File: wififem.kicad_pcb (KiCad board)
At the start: 2 copper layers, 31 parts, among them J1 Conn_Coaxial, J2 Conn_Coaxial, J3 Conn_Coaxial, J4 Conn_Coaxial, U1 MCP6566, U2 74HCT04, U3 SE2611T

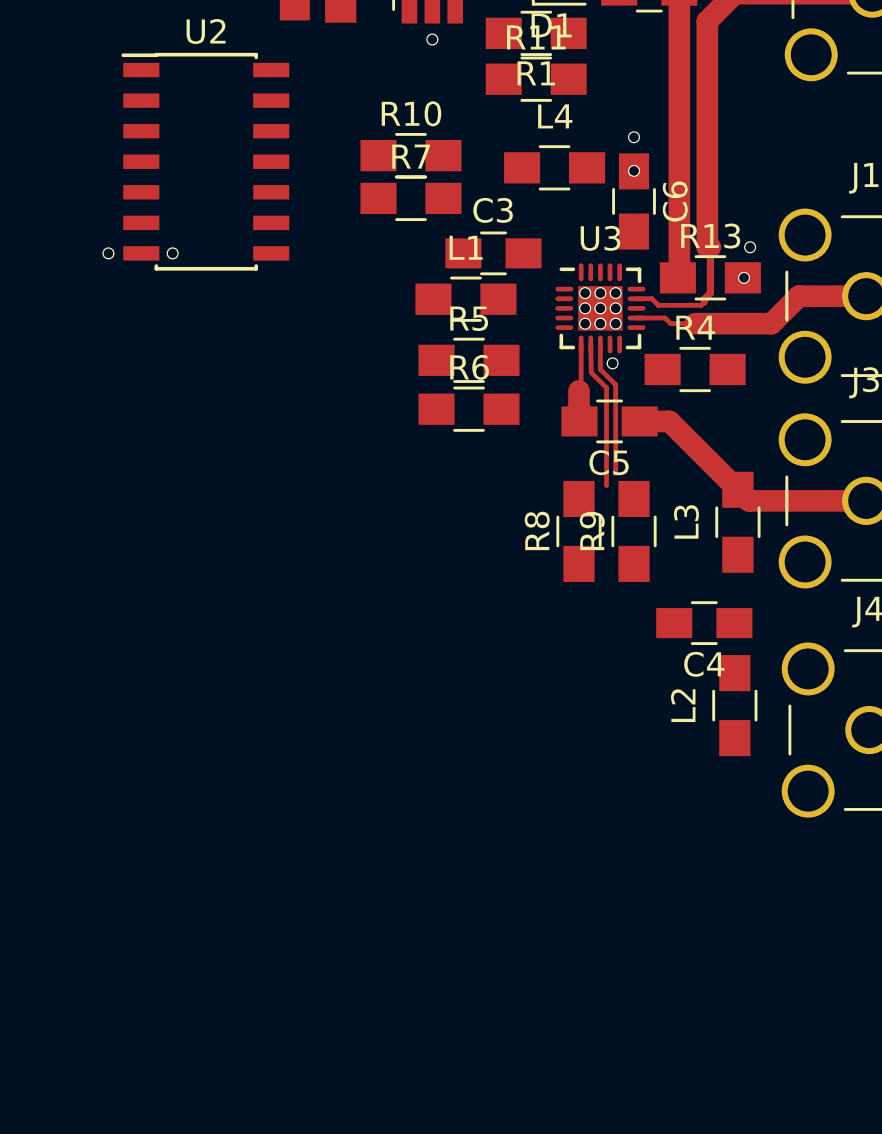
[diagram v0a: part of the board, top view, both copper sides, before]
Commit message: Add regulator in schematic, some progress with layout
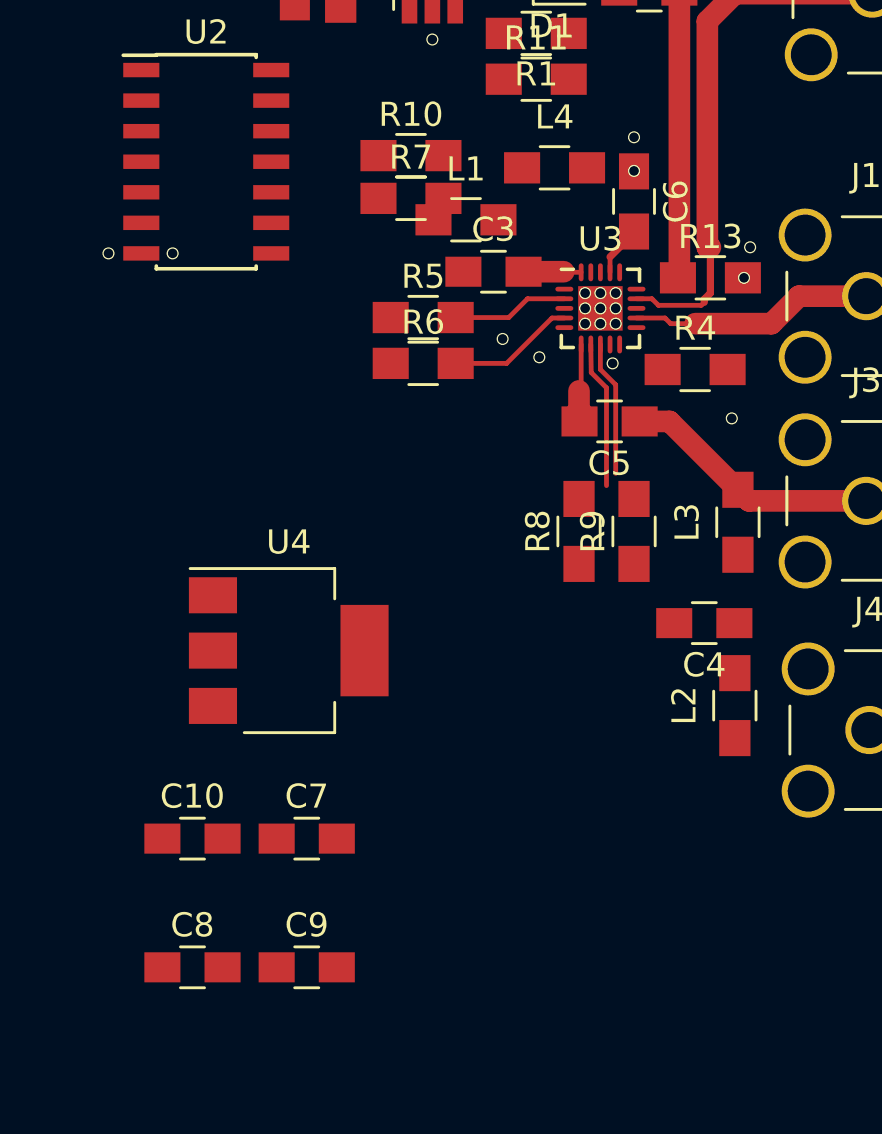
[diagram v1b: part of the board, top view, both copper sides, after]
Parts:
- added C10: 100n, Capacitors_SMD:C_0805_HandSoldering, F.Cu at (92.9, 87.4)
- added C7: 100n, Capacitors_SMD:C_0805_HandSoldering, F.Cu at (97.6, 87.4)
- added C8: 100n, Capacitors_SMD:C_0805_HandSoldering, F.Cu at (92.9, 92.8)
- added C9: 100n, Capacitors_SMD:C_0805_HandSoldering, F.Cu at (97.6, 92.8)
- added U4: AP1117-15, TO_SOT_Packages_SMD:SOT-223-3_TabPin2, F.Cu at (96.9, 79.6)
- moved L1 3.30 mm to (104.3, 61.7)
- moved R6 2.69 mm to (102.5, 67.7)
- moved R5 2.61 mm to (102.5, 65.8)
- moved C3 0.76 mm to (105.4, 63.9)
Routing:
- net Net-(R6-Pad2): track 0.00 -> 5.30 mm
- net Net-(R5-Pad2): track 0.00 -> 4.84 mm
- net Net-(C3-Pad2): track 0.00 -> 2.40 mm
- net Net-(C6-Pad2): track 0.00 -> 2.11 mm
- net GND: vias 20 -> 23

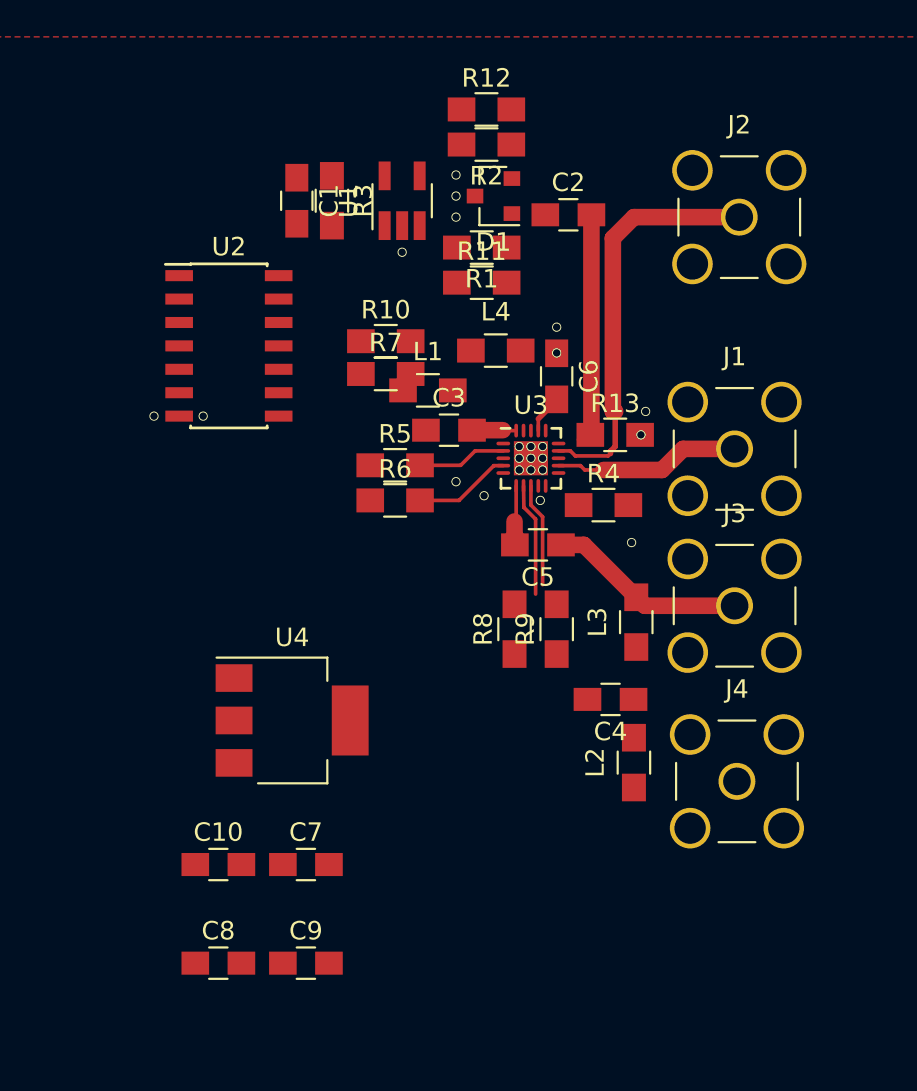
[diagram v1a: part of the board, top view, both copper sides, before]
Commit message: Replaced directional coupler with simple parallel connection. Layout almost done
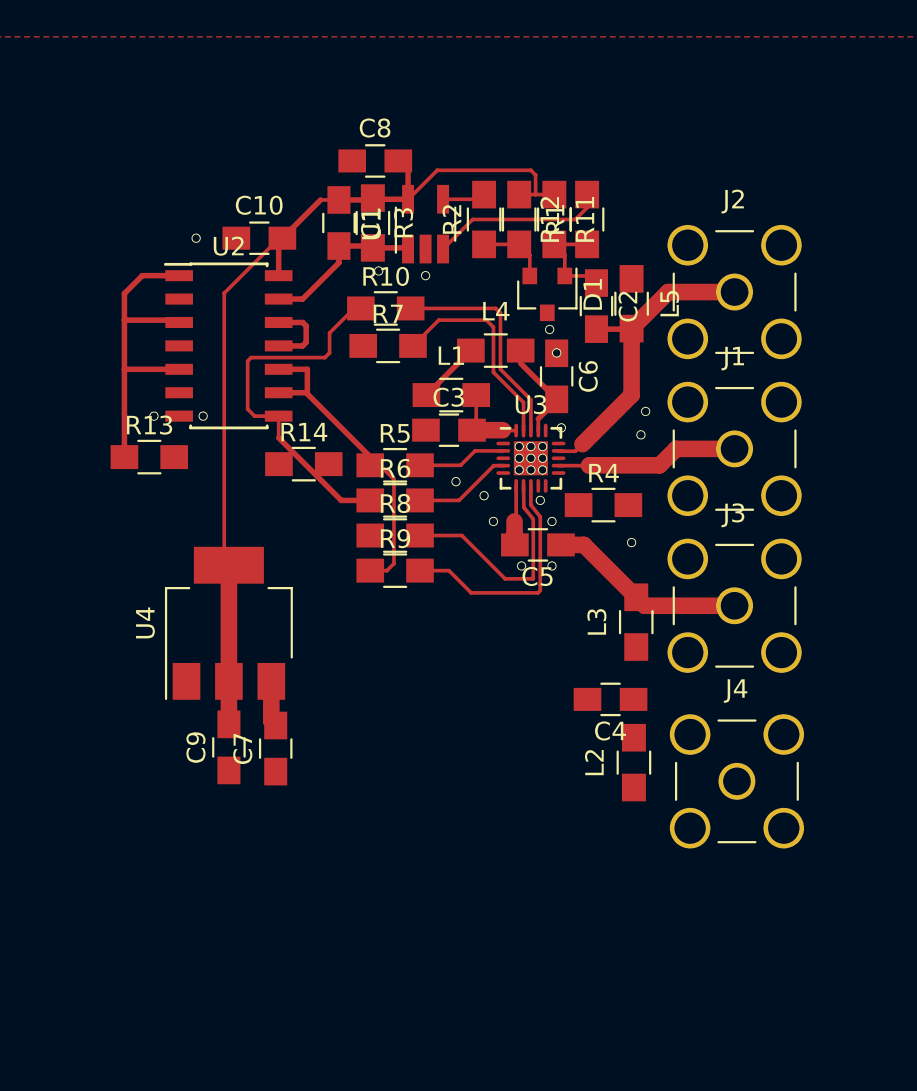
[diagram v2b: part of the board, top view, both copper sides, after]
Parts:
- added L5: 10n, Inductors_SMD:L_0805_HandSoldering, F.Cu at (115.3, 57.0)
- added R14: 0, Resistors_SMD:R_0805_HandSoldering, F.Cu at (97.5, 65.7)
- C2: value 10p -> 1p
- L1, L2, L3, L4: value INDUCTOR -> 2.4 GHz choke
- moved C8 44.3 mm to (101.4, 49.3)
- moved C10 34.0 mm to (95.1, 53.5)
- moved R13 25.3 mm to (89.2, 65.3)
- moved C9 12.4 mm to (93.5, 81.1), turned to 90 degrees
- moved R9 9.32 mm to (102.5, 71.5), turned to 0 degrees
- moved R8 8.23 mm to (102.5, 69.6), turned to 0 degrees
- moved C7 6.50 mm to (96.0, 81.2), turned to 90 degrees
- moved U4 6.29 mm to (93.5, 74.4), turned to 90 degrees
- moved R12 6.23 mm to (109.2, 52.5), turned to 270 degrees
- moved D1 6.08 mm to (110.7, 56.5), turned to 270 degrees
- moved R1 5.91 mm to (112.9, 52.5), turned to 90 degrees
- moved R11 5.22 mm to (111.1, 52.5), turned to 270 degrees
- moved C2 5.18 mm to (113.4, 57.1), turned to 270 degrees
- moved J2 4.07 mm to (120.9, 56.4)
- moved R2 4.07 mm to (107.3, 52.5), turned to 90 degrees
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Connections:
- J2 pad 1: Net-(J2-Pad1) -> Net-(C2-Pad2)
- L1 pad 1: +3V3 -> Net-(L1-Pad1)
- L4 pad 1: +3V3 -> Net-(L1-Pad1)
- R13 pad 1: Net-(C2-Pad2) -> Net-(R13-Pad1)
- U2 pad 1: Net-(C1-Pad2) -> Net-(R13-Pad1)
- U2 pad 10: (no net) -> Net-(R5-Pad1)
- U2 pad 11: (no net) -> Net-(U2-Pad11)
- U2 pad 12: (no net) -> Net-(U2-Pad11)
- U2 pad 13: (no net) -> Net-(C1-Pad2)
- U2 pad 3: Net-(U2-Pad2) -> Net-(R13-Pad1)
- U2 pad 4: Net-(R5-Pad1) -> Net-(U2-Pad4)
- U2 pad 5: Net-(R5-Pad1) -> Net-(R13-Pad1)
- U2 pad 6: Net-(R10-Pad1) -> Net-(U2-Pad6)
- U2 pad 8: (no net) -> Net-(R10-Pad1)
- U2 pad 9: (no net) -> Net-(R5-Pad1)
- U3 pad 14: Net-(J2-Pad1) -> Net-(C2-Pad2)
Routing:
- net +3V3: track 0.00 -> 50.6 mm
- net Net-(J2-Pad1): track 22.2 -> 0.00 mm
- net Net-(R10-Pad1): track 0.00 -> 20.0 mm
- net Net-(R13-Pad1): track 0.00 -> 18.2 mm
- net Net-(R5-Pad1): track 0.00 -> 17.5 mm
- net Net-(R10-Pad2): track 0.00 -> 12.0 mm
- net Net-(R7-Pad2): track 0.00 -> 11.4 mm
- net Net-(R1-Pad2): track 0.00 -> 9.46 mm
- net Net-(C1-Pad2): track 0.00 -> 8.81 mm, vias 0 -> 1
- net Net-(R9-Pad2): track 5.62 -> 12.9 mm
- net Net-(R8-Pad2): track 6.13 -> 12.3 mm
- net Net-(C2-Pad1): track 0.00 -> 5.60 mm
- net Net-(C2-Pad2): track 12.0 -> 17.2 mm
- net Net-(U2-Pad11): track 0.00 -> 4.03 mm
- net Net-(D1-Pad2): track 0.00 -> 3.86 mm
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
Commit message: Layout changes
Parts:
- moved C9 12.8 mm to (96.1, 68.6), turned to 180 degrees
- moved R8 6.22 mm to (108.7, 69.6)
- moved R9 6.22 mm to (108.7, 71.5)
- moved L2 3.72 mm to (114.2, 78.4), turned to 0 degrees
- moved C5 3.30 mm to (110.1, 73.4)
- moved C4 3.10 mm to (112.1, 76.2)
- moved R14 2.94 mm to (100.5, 65.4), turned to 90 degrees
- moved C7 2.67 mm to (93.6, 80.0), turned to 0 degrees
- moved R5 2.41 mm to (104.9, 65.8)
- moved R6 2.41 mm to (104.9, 67.7)
- moved L3 0.25 mm to (115.6, 74.5)
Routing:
- net Net-(R8-Pad2): track 12.3 -> 3.80 mm
- net Net-(R9-Pad2): track 12.9 -> 6.51 mm
- net +3V3: track 50.6 -> 56.1 mm
- net Net-(L1-Pad1): track 3.41 -> 8.00 mm
- net GND: track 0.00 -> 4.10 mm, vias 26 -> 24
- net Net-(R5-Pad1): track 17.5 -> 21.4 mm
- net Net-(C5-Pad2): track 2.99 -> 6.74 mm
- net Net-(R10-Pad1): track 20.0 -> 22.6 mm
- net Net-(R5-Pad2): track 4.84 -> 2.43 mm
- net Net-(R4-Pad1): track 0.00 -> 2.19 mm
- net Net-(R6-Pad2): track 5.30 -> 3.40 mm
- net Net-(C5-Pad1): track 10.8 -> 9.55 mm
- added copper zone on B.Cu, net GND

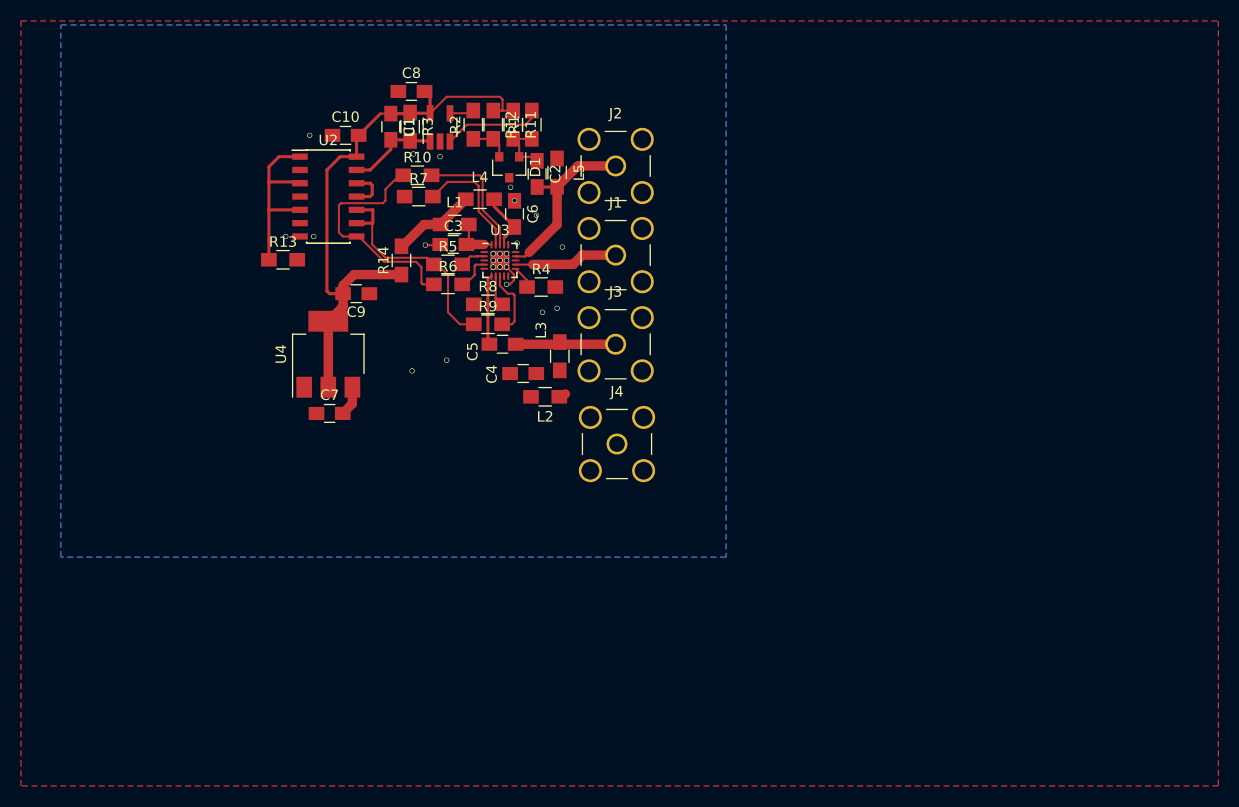
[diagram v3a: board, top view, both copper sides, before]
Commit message: RF layout improvement
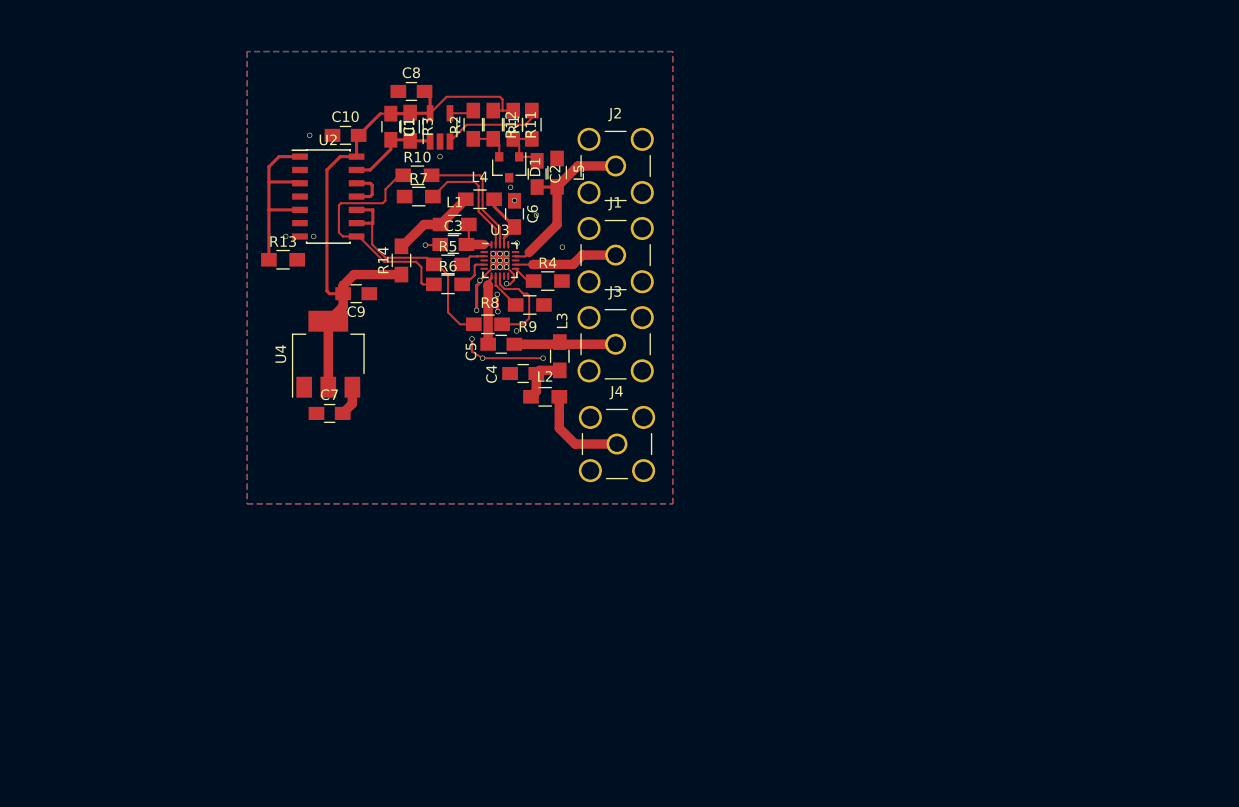
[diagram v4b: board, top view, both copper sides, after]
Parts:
- moved R8 4.00 mm to (112.7, 69.7), turned to 180 degrees
- moved R4 0.85 mm to (114.4, 67.4)
- moved C5 0.13 mm to (110.0, 73.4)
- turned L2 to 180 degrees
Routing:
- net GND: track 4.10 -> 19.0 mm, vias 24 -> 28
- net Net-(J4-Pad1): track 0.00 -> 9.13 mm
- net Net-(C4-Pad1): track 0.24 -> 5.01 mm
- net Net-(R9-Pad2): track 6.51 -> 9.01 mm
- net Net-(R4-Pad1): track 2.19 -> 2.86 mm
- net Net-(C1-Pad2): vias 1 -> 0

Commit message: Everything in layout, DRC passes
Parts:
- added D2: DIODE, Resistors_SMD:R_0805_HandSoldering, F.Cu at (96.9, 83.6)
- added L6: ferrite bead, Inductors_SMD:L_0805_HandSoldering, F.Cu at (116.7, 84.1)
- added MK1: Mounting_Hole_PAD, Mounting_Holes:MountingHole_3.2mm_M3_Pad, F.Cu at (121.3, 88.6)
- added MK2: Mounting_Hole_PAD, Mounting_Holes:MountingHole_3.2mm_M3_Pad, F.Cu at (90.8, 48.0)
- added MK3: Mounting_Hole_PAD, Mounting_Holes:MountingHole_3.2mm_M3_Pad, F.Cu at (121.3, 48.0)
- added MK4: Mounting_Hole_PAD, Mounting_Holes:MountingHole_3.2mm_M3_Pad, F.Cu at (90.8, 88.6)
- J4: value Conn_Coaxial -> Conn_01x05; footprint Connectors:SMA_THT_Jack_Straight -> Socket_Strips:Socket_Strip_Straight_1x05_Pitch2.54mm
- L1, L2, L4: value 2.4 GHz choke -> ferrite bead
- moved J4 7.61 mm to (113.7, 81.0), turned to 90 degrees
- moved U4 3.68 mm to (96.9, 75.7)
- moved C7 3.64 mm to (96.9, 81.5)
- moved R13 2.21 mm to (90.6, 67.1), turned to 270 degrees
- moved C9 1.57 mm to (94.6, 69.0), turned to 0 degrees
- moved L2 0.19 mm to (114.2, 78.2), turned to 0 degrees
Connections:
- J4 pad 1: Net-(J4-Pad1) -> GND
- J4 pad 2: GND -> Net-(J4-Pad2)
- L2 pad 1: Net-(J4-Pad1) -> Net-(C4-Pad1)
- L2 pad 2: Net-(C4-Pad1) -> Net-(J4-Pad2)
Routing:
- net Net-(C7-Pad2): track 2.88 -> 22.5 mm
- net GND: track 19.0 -> 8.45 mm, vias 28 -> 69
- net Net-(J4-Pad1): track 9.13 -> 0.00 mm
- net Net-(J4-Pad4): track 0.00 -> 4.93 mm
- net Net-(J4-Pad2): track 0.00 -> 3.08 mm
- net Net-(MK2-Pad1): track 0.00 -> 2.61 mm
- net Net-(R13-Pad1): track 18.2 -> 15.8 mm
- added copper zone on F.Cu, net +3V3
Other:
- board outline added: 40 x 48.3 mm
- net class Default: clearance 0.1 -> 0.1524
- rule trace_clearance: 0.1 -> 0.1524
- board text added: "2.4 GHz front-end OH2EAT 2017"
- board text added: "ANT"
- board text added: "DC"
- board text added: "RX"
- board text added: "TX"
